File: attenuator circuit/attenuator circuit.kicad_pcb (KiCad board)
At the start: 2 copper layers, 50.3 x 14.2 mm, 6 parts, among them J1 SJ1-3525N, J2 SJ1-3525N

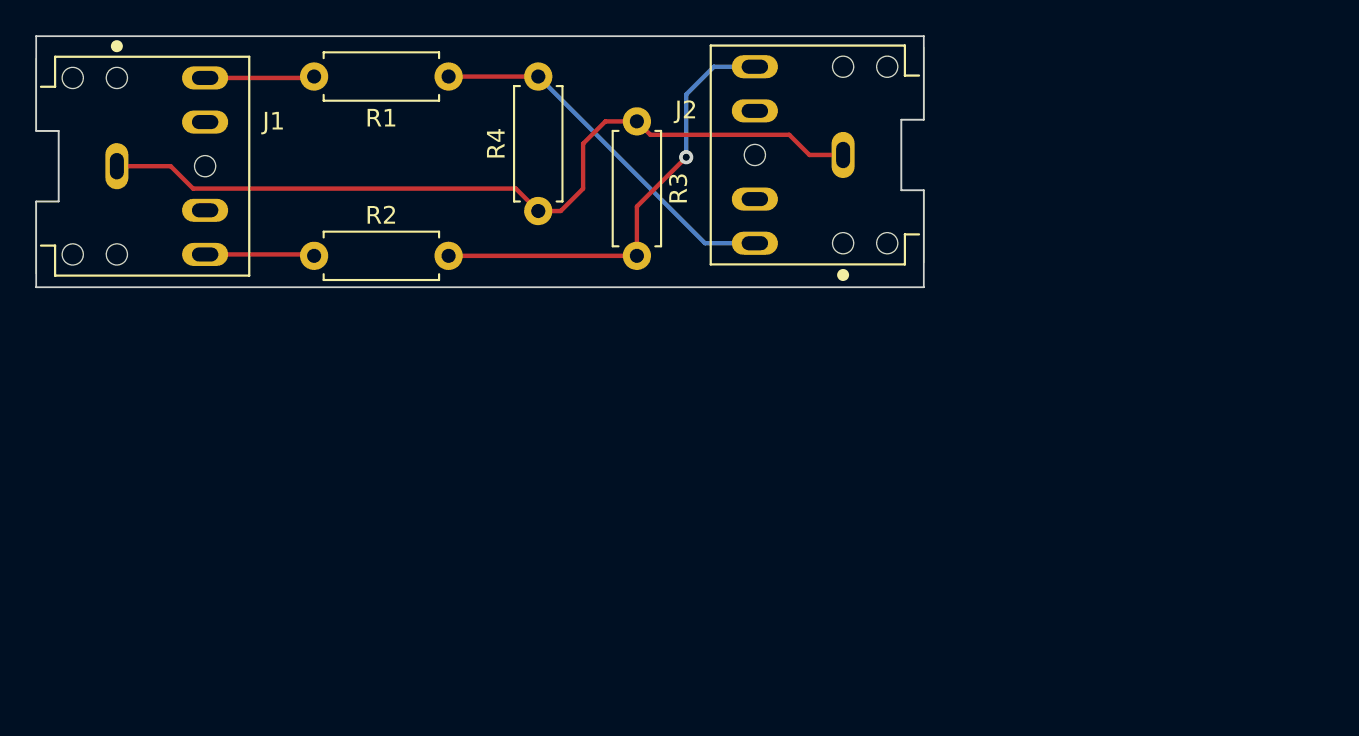
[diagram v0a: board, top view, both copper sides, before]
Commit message: Version 2 of PCB
- re-arrange things to be more uniform
- shorten it slightly (Save $0.25! )
- widen the trace size
- makes use of a ground plane
- add some fancy labels
- label the resistors with actual values for most common scenario
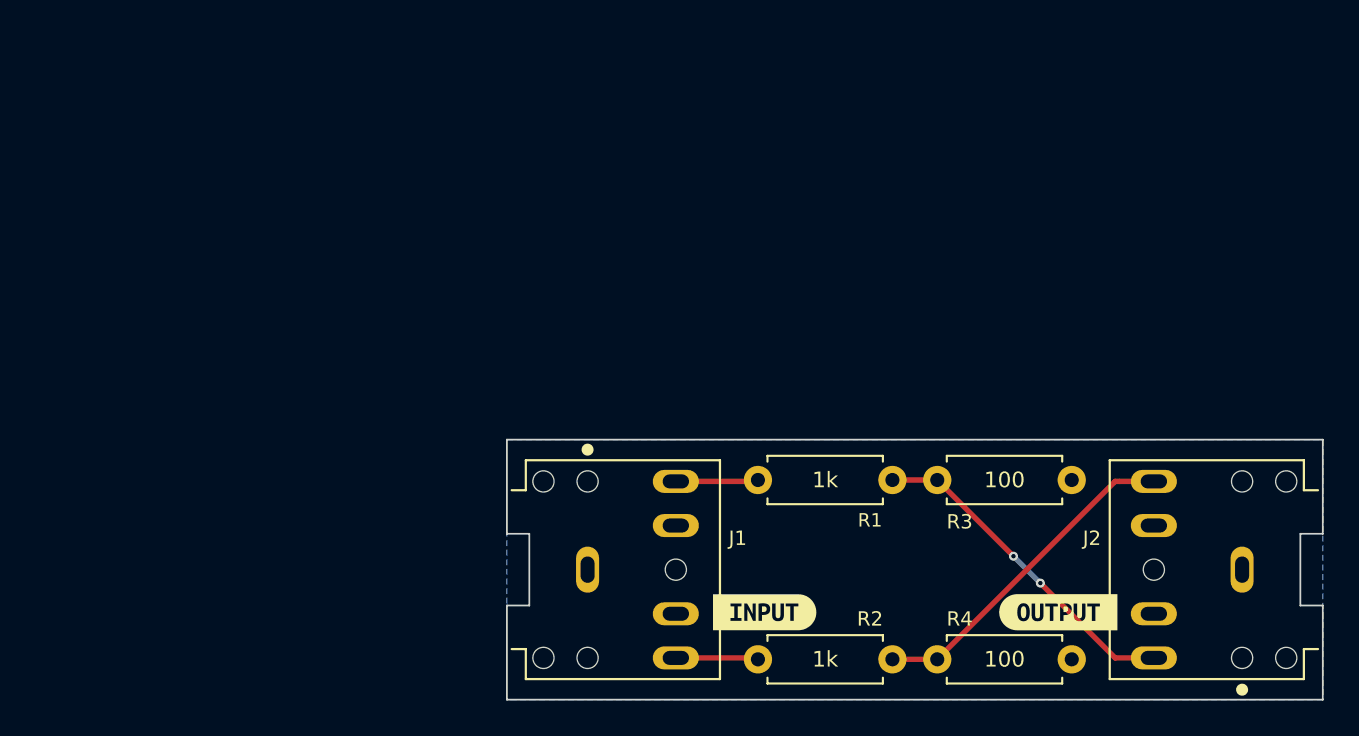
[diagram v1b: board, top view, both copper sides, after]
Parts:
- removed the R3 at (125.0, 75.2)
- added R4: 100, Resistor_THT:R_Axial_DIN0207_L6.3mm_D2.5mm_P7.62mm_Horizontal, F.Cu at (142.0, 105.7)
- added kibuzzard-614ACF93: G***, label, F.Cu at (148.8, 103.0)
- added kibuzzard-614AD03C: G***, label, F.Cu at (132.2, 103.0)
- added kibuzzard-614AD37E: G***, label, B.Cu at (132.5, 103.1)
- added kibuzzard-614AD392: G***, label, B.Cu at (148.6, 103.1)
- added kibuzzard-614ADC34: G***, label, B.Cu at (140.7, 97.9)
- J1: value SJ1-3525N -> INPUT
- J2: value SJ1-3525N -> OUTPUT
- R1, R2: value 42 -> 1k
- R3: renamed from R4; value 420 -> 100
- moved J1 35.1 mm to (122.2, 100.6)
- moved R1 34.0 mm to (139.4, 95.5)
- moved R2 34.0 mm to (139.4, 105.7)
- moved R3 33.9 mm to (149.6, 95.5), turned to 180 degrees
- moved J2 32.6 mm to (159.3, 100.6)
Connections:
- net Net-(J1-Pad1) renamed /GND
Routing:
- net /GND: track 46.6 -> 0.00 mm
- net Net-(J2-Pad2): track 25.5 -> 19.0 mm, vias 1 -> 0
- net Net-(J2-Pad3): track 21.3 -> 19.0 mm, vias 0 -> 2
- net Net-(J1-Pad3): track 6.21 -> 4.69 mm
- net Net-(J1-Pad2): track 6.21 -> 4.69 mm
- added copper zone on B.Cu, net /GND
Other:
- board size 50.3 x 14.2 mm -> 46.2 x 14.7 mm
- board text added: "By Todd Eddy"
- board text added: "git.io/JzR8k"
- board text added: "v2 2021-09-24"
- board text removed: "AUDIO ATTENUATOR v1 2021-09-05"
- board text removed: "IN"
- board text removed: "OUT"
